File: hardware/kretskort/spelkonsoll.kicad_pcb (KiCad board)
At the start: 2 copper layers, 2 parts, among them U2 ESP32-DEVKITC-32D, U3 ILI9488

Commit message: more circuit board kicad files
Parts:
- added BZ1: Buzzer, Buzzer_Beeper:Buzzer_15x7.5RM7.6, F.Cu at (204.8, 113.8)
- added SW1: SW_Push, Button_Switch_THT:SW_TH_Tactile_Omron_B3F-10xx, F.Cu at (217.4, 90.8)
- added SW10: SW_Push, Button_Switch_THT:SW_TH_Tactile_Omron_B3F-10xx, F.Cu at (79.3, 118.0)
- added SW11: SW_Push, Button_Switch_THT:SW_Tactile_SPST_Angled_PTS645Vx83-2LFS, F.Cu at (89.2, 72.1)
- added SW12: SW_Push, Button_Switch_THT:SW_Tactile_SPST_Angled_PTS645Vx83-2LFS, F.Cu at (197.0, 72.1)
- added SW2: SW_Push, Button_Switch_THT:SW_TH_Tactile_Omron_B3F-10xx, F.Cu at (206.4, 95.4)
- added SW3: SW_Push, Button_Switch_THT:SW_TH_Tactile_Omron_B3F-10xx, F.Cu at (197.5, 90.8)
- added SW4: SW_Push, Button_Switch_THT:SW_TH_Tactile_Omron_B3F-10xx, F.Cu at (206.4, 75.6)
- added SW5: SW_Push, Button_Switch_THT:SW_TH_Tactile_Omron_B3F-10xx, F.Cu at (78.9, 78.1)
- added SW6: SW_Push, Button_Switch_THT:SW_TH_Tactile_Omron_B3F-10xx, F.Cu at (78.9, 93.5)
- added SW7: SW_Push, Button_Switch_THT:SW_TH_Tactile_Omron_B3F-10xx, F.Cu at (88.3, 91.3)
- added SW8: SW_Push, Button_Switch_THT:SW_TH_Tactile_Omron_B3F-10xx, F.Cu at (71.5, 91.3)
- added SW9: SW_Push, Button_Switch_THT:SW_TH_Tactile_Omron_B3F-10xx, F.Cu at (79.3, 108.3)
- moved U3 19.0 mm to (150.2, 106.6)
- moved U2 17.1 mm to (160.2, 110.6)
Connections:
- U2 pad 10: Net-(U2-Pad10) -> BTN_SELECT
- U2 pad 11: Net-(U2-Pad11) -> BTN_DP_UP
- U2 pad 12: Net-(U2-Pad12) -> BTN_DP_DOWN
- U2 pad 13: Net-(U2-Pad13) -> BTN_DP_LEFT
- U2 pad 15: Net-(U2-Pad15) -> BTN_DP_RIGHT
- U2 pad 18: GND -> Net-(U2-Pad18)
- U2 pad 25: Net-(U2-Pad25) -> BUZZER
- U2 pad 30: Net-(U2-Pad30) -> BTN_BUMPER_L
- U2 pad 31: Net-(U2-Pad31) -> BTN_BUMPER_R
- U2 pad 5: Net-(U2-Pad5) -> BTN_A
- U2 pad 6: Net-(U2-Pad6) -> BTN_B
- U2 pad 7: Net-(U2-Pad7) -> BTN_X
- U2 pad 8: Net-(U2-Pad8) -> BTN_Y
- U2 pad 9: Net-(U2-Pad9) -> BTN_START
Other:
- board outline added: 170.1 x 56.6 mm

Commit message: more circuit board kicad files
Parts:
- moved SW11 1.07 mm to (88.2, 72.4)
- moved SW12 0.59 mm to (197.4, 72.4)
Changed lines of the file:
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@@
     (solder_mask_min_width 0.25)
     (aux_axis_origin 0 0)
+    (grid_origin 146.05 92.71)
     (visible_elements FFFFFF7F)
     (pcbplotparams
@@
   )
   (module Button_Switch_THT:SW_Tactile_SPST_Angled_PTS645Vx83-2LFS (layer F.Cu)
-    (at 89.22346 72.0725)
+    (at 88.22 72.44)
     (descr "tactile switch SPST right angle, PTS645VL83-2 LFS")
     (tags "tactile switch SPST angled PTS645VL83-2 LFS C&K Button")
@@
   )
   (module Button_Switch_THT:SW_Tactile_SPST_Angled_PTS645Vx83-2LFS (layer F.Cu)
-    (at 196.97192 72.08266)
+    (at 197.44 72.44)
     (descr "tactile switch SPST right angle, PTS645VL83-2 LFS")
     (tags "tactile switch SPST angled PTS645VL83-2 LFS C&K Button")
@@
       (effects (font (size 1 1) (thickness 0.15)))
     )
+    (fp_line (start 0.5 -8.35) (end 0.5 -2.59) (layer F.Fab) (width 0.1))
+    (fp_line (start 4 -8.35) (end 4 -2.59) (layer F.Fab) (width 0.1))
+    (fp_line (start 0.5 -8.35) (end 4 -8.35) (layer F.Fab) (width 0.1))
+    (fp_text user %R (at 2.25 1.68) (layer F.Fab)
+      (effects (font (size 1 1) (thickness 0.15)))
+    )
+    (fp_line (start -1.09 0.97) (end -1.09 1.2) (layer F.SilkS) (width 0.12))
+    (fp_line (start 5.7 4.2) (end 5.7 0.86) (layer F.Fab) (width 0.1))
+    (fp_line (start -1.5 4.2) (end -1.2 4.2) (layer F.Fab) (width 0.1))
+    (fp_line (start -1.2 0.86) (end 5.7 0.86) (layer F.Fab) (width 0.1))
+    (fp_line (start 6 4.2) (end 6 -2.59) (layer F.Fab) (width 0.1))
+    (fp_line (start -2.5 -2.8) (end 7.05 -2.8) (layer F.CrtYd) (width 0.05))
+    (fp_line (start 7.05 -2.8) (end 7.05 4.45) (layer F.CrtYd) (width 0.05))
+    (fp_line (start 7.05 4.45) (end -2.5 4.45) (layer F.CrtYd) (width 0.05))
+    (fp_line (start -2.5 4.45) (end -2.5 -2.8) (layer F.CrtYd) (width 0.05))
+    (fp_line (start -1.61 -2.7) (end 6.11 -2.7) (layer F.SilkS) (width 0.12))
+    (fp_line (start 6.11 -2.7) (end 6.11 1.2) (layer F.SilkS) (width 0.12))
+    (fp_line (start -1.61 4.31) (end -1.09 4.31) (layer F.SilkS) (width 0.12))
+    (fp_line (start -1.61 -2.7) (end -1.61 1.2) (layer F.SilkS) (width 0.12))
+    (fp_line (start -1.5 -2.59) (end 6 -2.59) (layer F.Fab) (width 0.1))
+    (fp_line (start -1.5 4.2) (end -1.5 -2.59) (layer F.Fab) (width 0.1))
+    (fp_line (start 5.7 4.2) (end 6 4.2) (layer F.Fab) (width 0.1))
+    (fp_line (start -1.2 4.2) (end -1.2 0.86) (layer F.Fab) (width 0.1))
+    (fp_line (start 5.59 0.97) (end 5.59 1.2) (layer F.SilkS) (width 0.12))
+    (fp_line (start -1.09 3.8) (end -1.09 4.31) (layer F.SilkS) (width 0.12))
+    (fp_line (start -1.61 3.8) (end -1.61 4.31) (layer F.SilkS) (width 0.12))
+    (fp_line (start 5.05 0.97) (end 5.59 0.97) (layer F.SilkS) (width 0.12))
+    (fp_line (start 5.59 3.8) (end 5.59 4.31) (layer F.SilkS) (width 0.12))
+    (fp_line (start 5.59 4.31) (end 6.11 4.31) (layer F.SilkS) (width 0.12))
+    (fp_line (start 6.11 3.8) (end 6.11 4.31) (layer F.SilkS) (width 0.12))
+    (fp_line (start -1.09 0.97) (end -0.55 0.97) (layer F.SilkS) (width 0.12))
     (fp_line (start 0.55 0.97) (end 3.95 0.97) (layer F.SilkS) (width 0.12))
-    (fp_line (start -1.09 0.97) (end -0.55 0.97) (layer F.SilkS) (width 0.12))
-    (fp_line (start 6.11 3.8) (end 6.11 4.31) (layer F.SilkS) (width 0.12))
-    (fp_line (start 5.59 4.31) (end 6.11 4.31) (layer F.SilkS) (width 0.12))
-    (fp_line (start 5.59 3.8) (end 5.59 4.31) (layer F.SilkS) (width 0.12))
-    (fp_line (start 5.05 0.97) (end 5.59 0.97) (layer F.SilkS) (width 0.12))
-    (fp_line (start -1.61 3.8) (end -1.61 4.31) (layer F.SilkS) (width 0.12))
-    (fp_line (start -1.09 3.8) (end -1.09 4.31) (layer F.SilkS) (width 0.12))
-    (fp_line (start 5.59 0.97) (end 5.59 1.2) (layer F.SilkS) (width 0.12))
-    (fp_line (start -1.2 4.2) (end -1.2 0.86) (layer F.Fab) (width 0.1))
-    (fp_line (start 5.7 4.2) (end 6 4.2) (layer F.Fab) (width 0.1))
-    (fp_line (start -1.5 4.2) (end -1.5 -2.59) (layer F.Fab) (width 0.1))
-    (fp_line (start -1.5 -2.59) (end 6 -2.59) (layer F.Fab) (width 0.1))
-    (fp_line (start -1.61 -2.7) (end -1.61 1.2) (layer F.SilkS) (width 0.12))
-    (fp_line (start -1.61 4.31) (end -1.09 4.31) (layer F.SilkS) (width 0.12))
-    (fp_line (start 6.11 -2.7) (end 6.11 1.2) (layer F.SilkS) (width 0.12))
-    (fp_line (start -1.61 -2.7) (end 6.11 -2.7) (layer F.SilkS) (width 0.12))
-    (fp_line (start -2.5 4.45) (end -2.5 -2.8) (layer F.CrtYd) (width 0.05))
-    (fp_line (start 7.05 4.45) (end -2.5 4.45) (layer F.CrtYd) (width 0.05))
-    (fp_line (start 7.05 -2.8) (end 7.05 4.45) (layer F.CrtYd) (width 0.05))
-    (fp_line (start -2.5 -2.8) (end 7.05 -2.8) (layer F.CrtYd) (width 0.05))
-    (fp_line (start 6 4.2) (end 6 -2.59) (layer F.Fab) (width 0.1))
-    (fp_line (start -1.2 0.86) (end 5.7 0.86) (layer F.Fab) (width 0.1))
-    (fp_line (start -1.5 4.2) (end -1.2 4.2) (layer F.Fab) (width 0.1))
-    (fp_line (start 5.7 4.2) (end 5.7 0.86) (layer F.Fab) (width 0.1))
-    (fp_line (start -1.09 0.97) (end -1.09 1.2) (layer F.SilkS) (width 0.12))
-    (fp_text user %R (at 2.25 1.68) (layer F.Fab)
-      (effects (font (size 1 1) (thickness 0.15)))
-    )
-    (fp_line (start 0.5 -8.35) (end 4 -8.35) (layer F.Fab) (width 0.1))
-    (fp_line (start 4 -8.35) (end 4 -2.59) (layer F.Fab) (width 0.1))
-    (fp_line (start 0.5 -8.35) (end 0.5 -2.59) (layer F.Fab) (width 0.1))
-    (pad "" thru_hole circle (at -1.25 2.49) (size 2.1 2.1) (drill 1.3) (layers *.Cu *.Mask))
+    (pad "" thru_hole circle (at 5.76 2.49) (size 2.1 2.1) (drill 1.3) (layers *.Cu *.Mask))
+    (pad 2 thru_hole circle (at 4.5 0) (size 1.75 1.75) (drill 0.99) (layers *.Cu *.Mask)
+      (net 1 +5V))
     (pad 1 thru_hole circle (at 0 0) (size 1.75 1.75) (drill 0.99) (layers *.Cu *.Mask)
       (net 45 BTN_BUMPER_R))
-    (pad 2 thru_hole circle (at 4.5 0) (size 1.75 1.75) (drill 0.99) (layers *.Cu *.Mask)
-      (net 1 +5V))
-    (pad "" thru_hole circle (at 5.76 2.49) (size 2.1 2.1) (drill 1.3) (layers *.Cu *.Mask))
+    (pad "" thru_hole circle (at -1.25 2.49) (size 2.1 2.1) (drill 1.3) (layers *.Cu *.Mask))
     (model ${KISYS3DMOD}/Button_Switch_THT.3dshapes/SW_Tactile_SPST_Angled_PTS645Vx83-2LFS.wrl
       (at (xyz 0 0 0))

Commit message: modified pcb to fit new design
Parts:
- added G***: LOGO, kretskort:hs_logo, B.Cu at (116.8, 110.5)
- added REF**: BatteryHolder_MPD_BH-18650-PC2, Battery:BatteryHolder_MPD_BH-18650-PC2, B.Cu at (109.5, 82.0)
- moved SW12 18.5 mm to (202.4, 54.6)
- moved SW8 17.2 mm to (88.7, 92.7)
- moved SW7 15.2 mm to (73.2, 92.7)
- moved SW5 9.59 mm to (86.5, 84.0), turned to 180 degrees
- moved SW6 9.56 mm to (86.5, 99.4), turned to 180 degrees
- moved SW9 7.75 mm to (85.9, 112.5), turned to 180 degrees
- moved SW10 7.12 mm to (85.9, 120.7), turned to 180 degrees
- moved SW3 5.10 mm to (198.8, 95.7)
- moved SW1 4.94 mm to (218.1, 95.7)
- moved SW4 4.86 mm to (207.5, 80.3)
- moved SW2 4.56 mm to (207.5, 99.8)
- moved U2 0.75 mm to (159.5, 110.5)
- moved SW11 0.68 mm to (88.9, 72.4)
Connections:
- SW1 pad 2: +5V -> GND
- SW10 pad 2: +5V -> GND
- SW11 pad 2: +5V -> GND
- SW12 pad 2: +5V -> GND
- SW2 pad 2: +5V -> GND
- SW3 pad 2: +5V -> GND
- SW4 pad 2: +5V -> GND
- SW5 pad 2: +5V -> GND
- SW6 pad 2: +5V -> GND
- SW7 pad 2: +5V -> GND
- SW8 pad 2: +5V -> GND
- SW9 pad 2: +5V -> GND
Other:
- board size 170.1 x 56.6 mm -> 167.2 x 56.6 mm
- net class Default: trace_width 0.25 -> 0.254; via_dia 0.8 -> 0.762; via_drill 0.4 -> 0.381
- board text added: "HACKERSPACE"

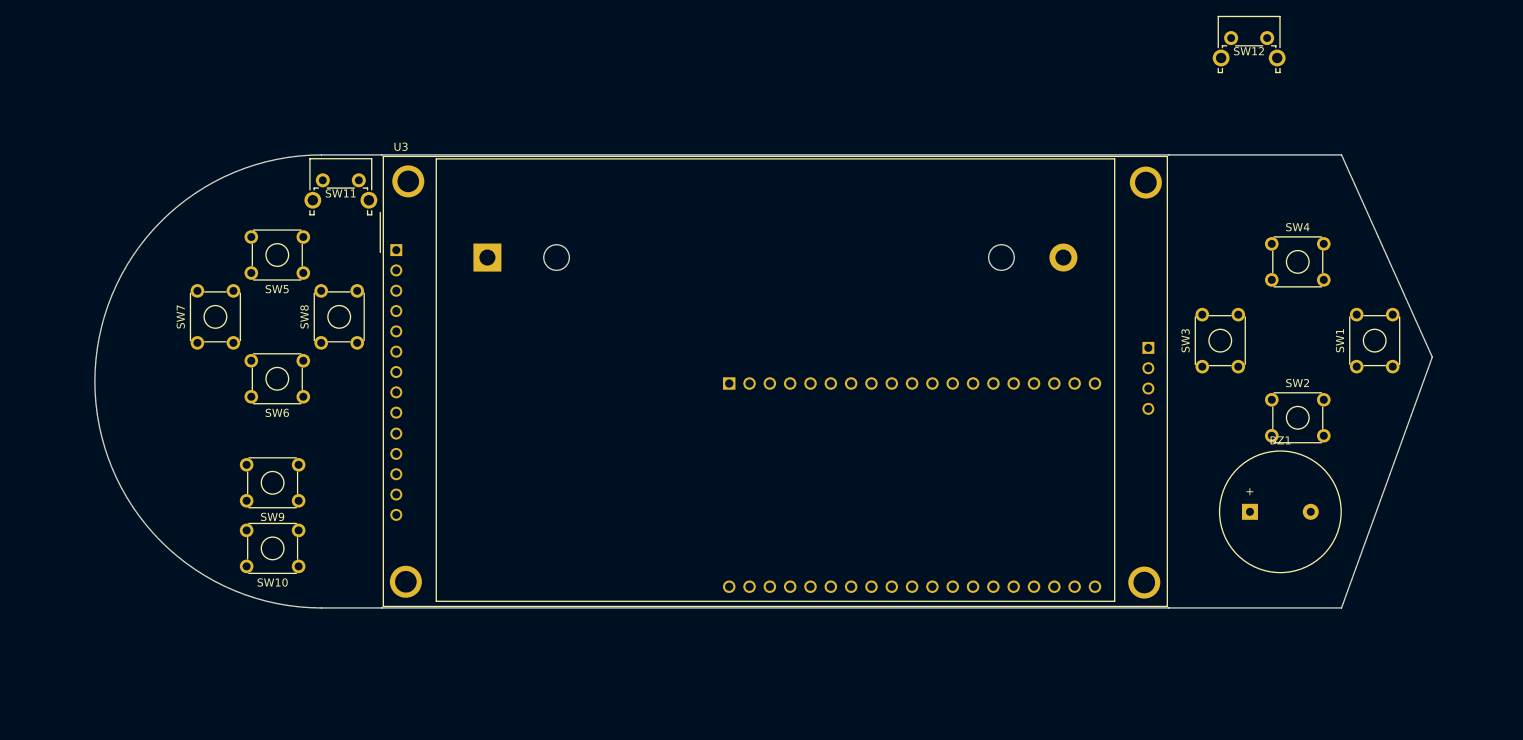
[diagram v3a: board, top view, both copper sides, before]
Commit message: fixed DRC error
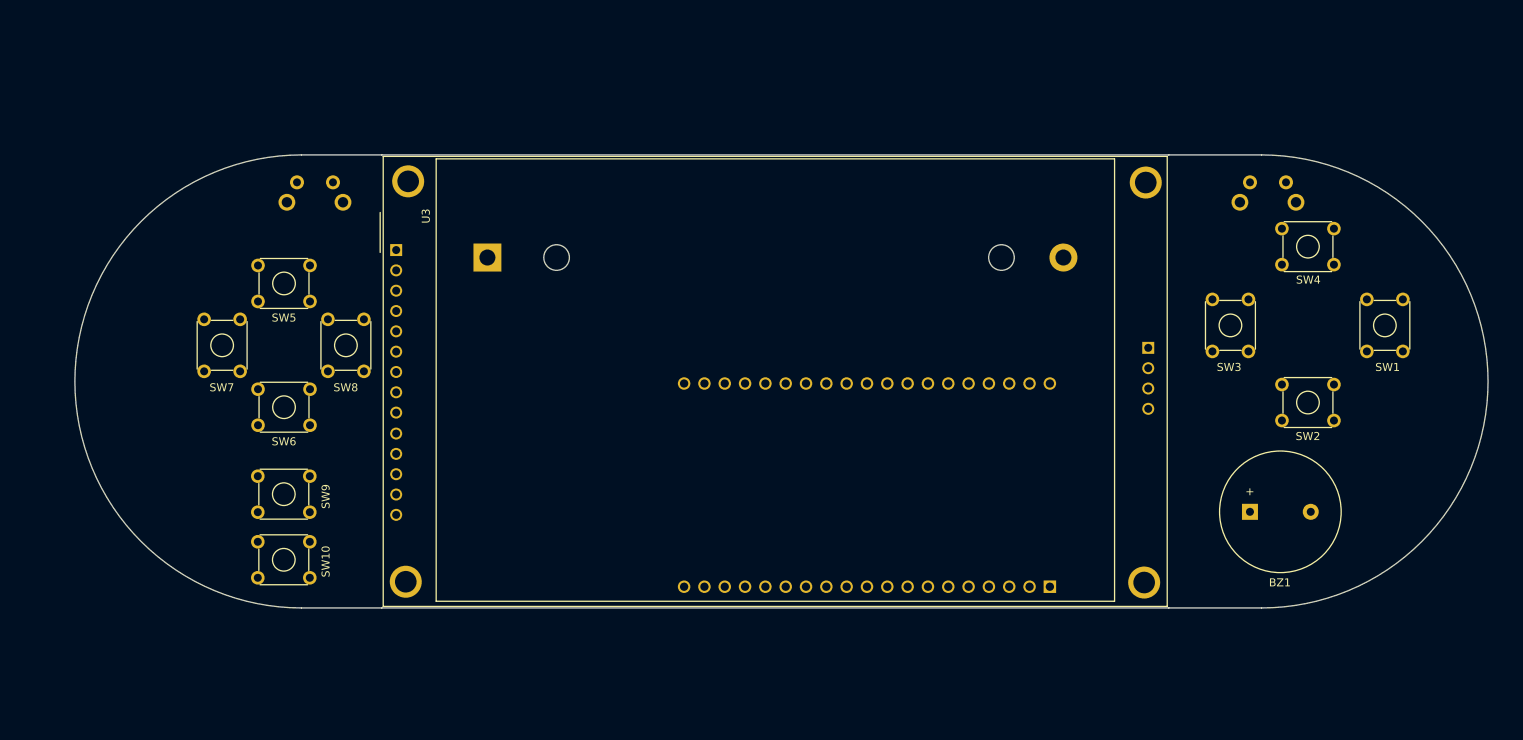
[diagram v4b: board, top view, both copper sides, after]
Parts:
- SW11, SW12: moved to B.Cu
- moved SW12 19.3 mm to (209.3, 72.6), turned to 180 degrees
- moved SW7 3.65 mm to (74.1, 96.3)
- moved SW8 3.65 mm to (89.5, 96.3)
- moved SW5 3.65 mm to (87.3, 87.5)
- moved SW6 3.65 mm to (87.3, 103.0)
- moved SW1 2.29 mm to (219.4, 93.8)
- moved SW2 2.29 mm to (208.8, 97.9)
- moved SW3 2.29 mm to (200.1, 93.8)
- moved SW4 2.29 mm to (208.8, 78.4)
- moved SW10 1.99 mm to (87.3, 122.1)
- moved SW9 1.99 mm to (87.3, 113.9)
- moved SW11 1.30 mm to (90.2, 72.6), turned to 180 degrees
- moved U2 0.56 mm to (160.0, 110.5), turned to 90 degrees
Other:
- board size 167.2 x 56.6 mm -> 176.6 x 56.6 mm

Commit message: added power circuit
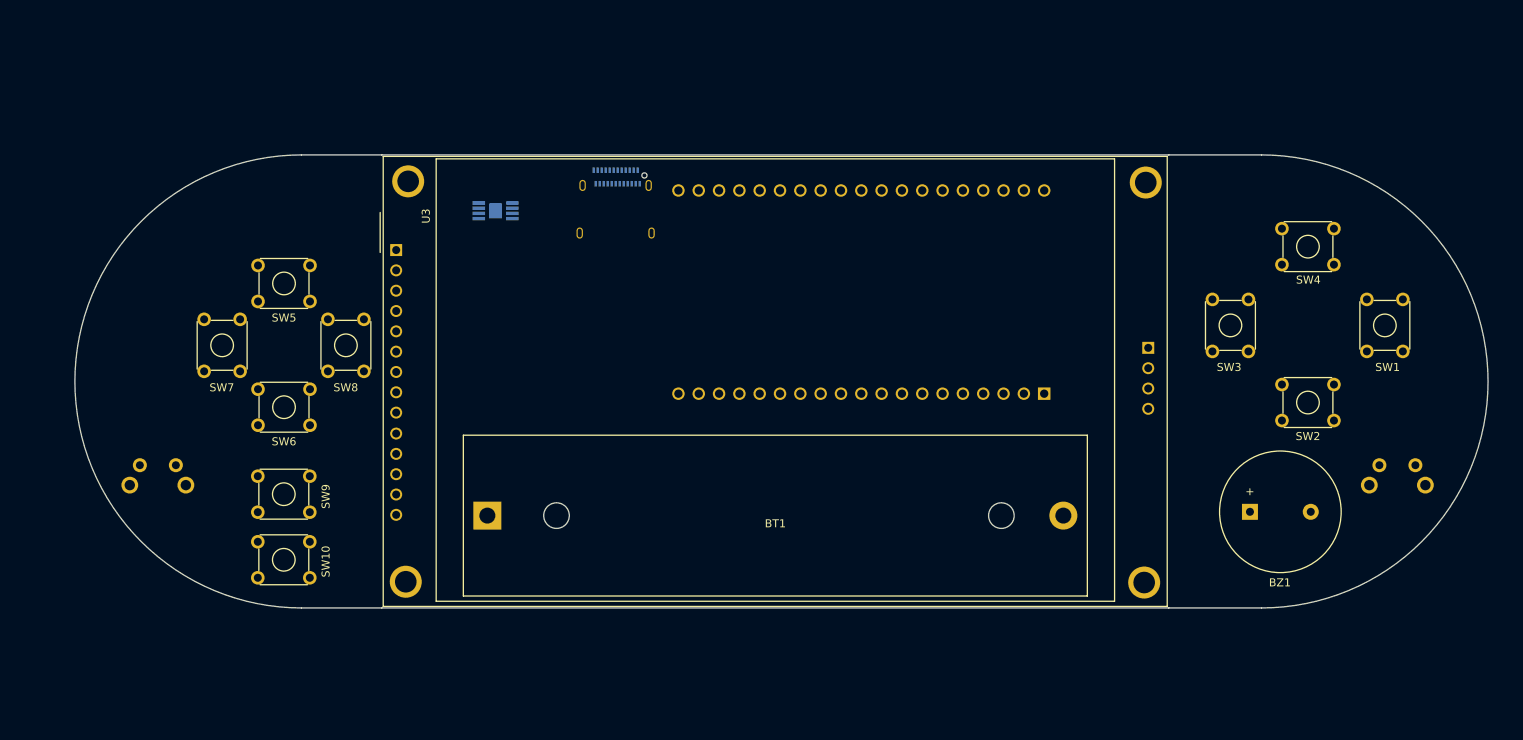
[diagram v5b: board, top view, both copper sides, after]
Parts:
- removed REF**: BatteryHolder_MPD_BH-18650-PC2, Battery:BatteryHolder_MPD_BH-18650-PC2
- added BT1: Battery_Cell, Battery:BatteryHolder_MPD_BH-18650-PC2, F.Cu at (109.5, 114.3)
- added J1: USB_C_Receptacle_USB2.0, Connector_USB:USB_C_Receptacle_Amphenol_12401610E4-2A, B.Cu at (125.5, 76.1)
- added U1: BQ24202DGN, Strøm:BQ24202DGN, B.Cu at (110.5, 76.2)
- moved SW11 40.4 mm to (70.5, 108.0)
- moved SW12 38.9 mm to (225.5, 108.0)
- moved U2 24.1 mm to (159.3, 86.4)
- moved G*** 19.0 mm to (116.8, 91.4)
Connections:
- U3 pad 8: Net-(U3-Pad8) -> +5V

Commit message: lol glemte å lagre
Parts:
- BT1: moved to B.Cu
- moved U1 17.2 mm to (124.8, 85.6)
- moved G*** 7.73 mm to (109.2, 92.7)
- moved J1 1.29 mm to (124.8, 75.0), turned to 0 degrees
